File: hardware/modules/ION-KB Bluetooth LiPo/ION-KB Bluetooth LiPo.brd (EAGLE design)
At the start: 38.1 x 54.8 mm, 4 parts, among them IC1 BLUETOOTH-RN42", U1 MCP73831

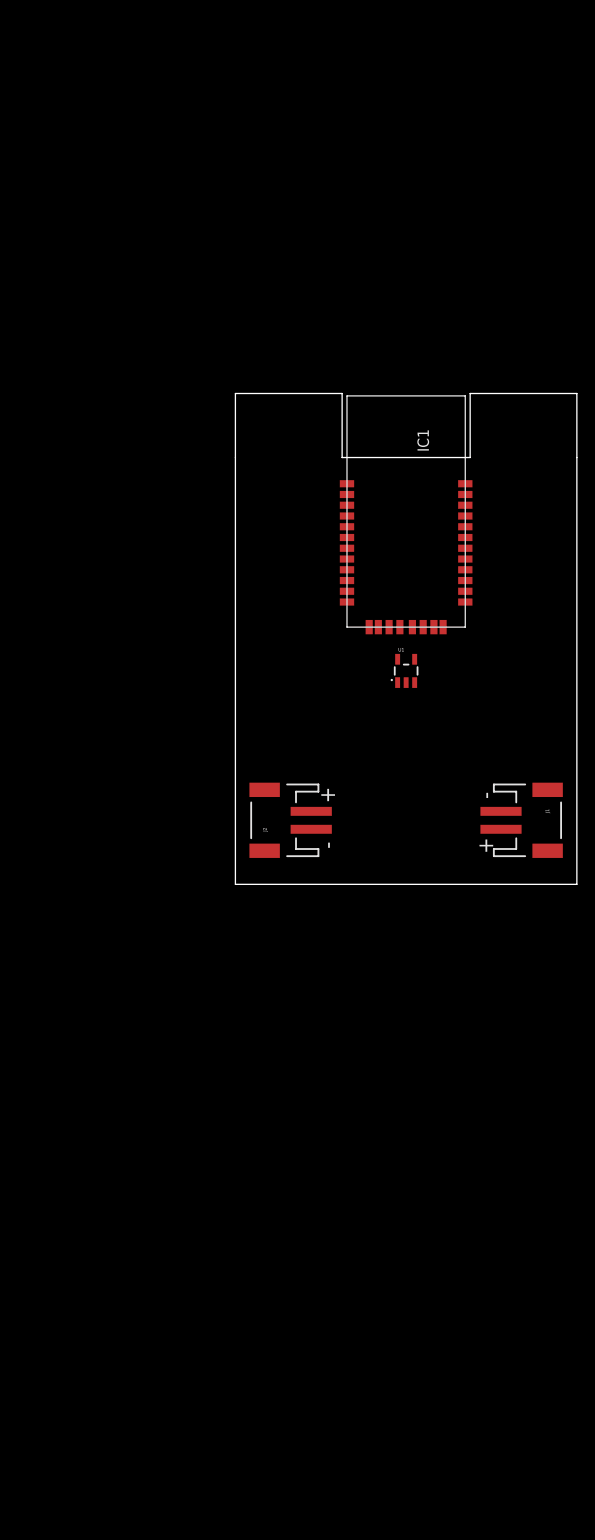
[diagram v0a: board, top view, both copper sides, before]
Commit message: Update bluetooth module
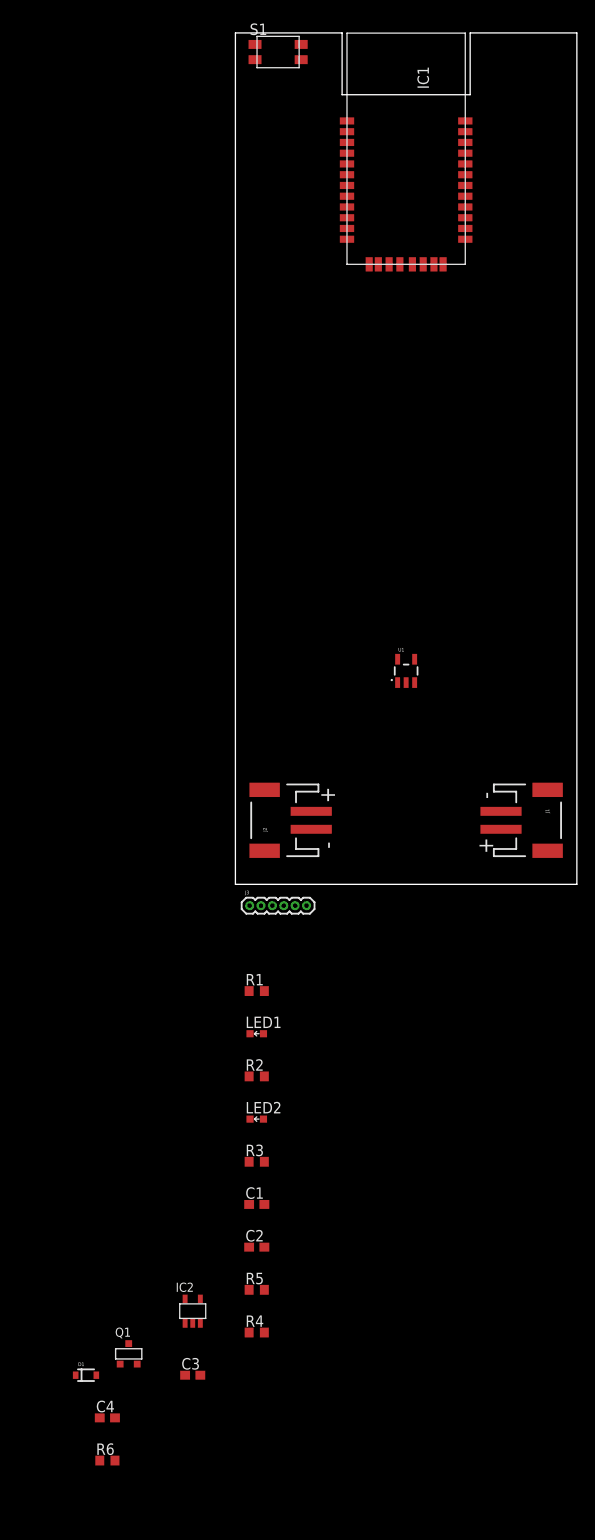
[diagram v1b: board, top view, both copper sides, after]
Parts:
- added C1, C2: 10uF, Jordi:C0603
- added C3: 470pF, Jordi:C0603
- added C4: 1uF, Jordi:C0603
- added D1: BAT20J, SparkFun-DiscreteSemi:SOD-323
- added IC2: VREG-5SOT23, Jordi:SOT23-5
- added J3: (no value), Jordi:M-1X06-0.05-PTH
- added LED1: Red, Jordi:L0603
- added LED2: Green, Jordi:L0603
- added Q1: MOSFET-PSUPERSOT, Jordi:SUPERSOT-3
- added R1, R4, R5: 10K, Jordi:R0603
- added R2, R3: 1K, Jordi:R0603
- added R6: 100K, Jordi:R0603
- added S1: (no value), Jordi:SWITCH-TACTILE-SMD
- moved IC1 40.5 mm to (19.1, 78.6)
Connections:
- removed net GND1: IC1.12
- removed net GND4: IC1.28
- removed net GND5: IC1.29
- removed net VDD: IC1.11
- removed net VSS: U1.2
- new net +3V3: IC1.11, IC2.4, J3.6, R5.2
- new net N$1: IC1.22, R1.2, S1.3, S1.4
- new net N$2: LED1.C, R2.2
- new net N$3: IC1.21, LED1.A
- new net N$4: IC1.19, LED2.A
- new net N$5: LED2.C, R3.2
- new net N$6: R4.1, U1.5
- new net N$8: C3.1, IC2.3
- new net STAT: R5.1, U1.1
- new net VCC: C4.2, D1.C, IC2.1, IC2.5, Q1.2
- net GND: now also C1.2, C2.1, C3.2, C4.1, IC1.12, IC1.28, IC1.29, IC2.2, J1.1, J2.1, J3.1, R1.1, R2.1, R3.1, R4.2, R6.1, S1.1, S1.2, U1.2
- net VBAT: now also C1.1, J1.2, J2.2, Q1.3
- net VIN: now also C2.2, D1.A, J3.5, Q1.1, R6.2
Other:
- board size 38.1 x 54.8 mm -> 38.1 x 95 mm

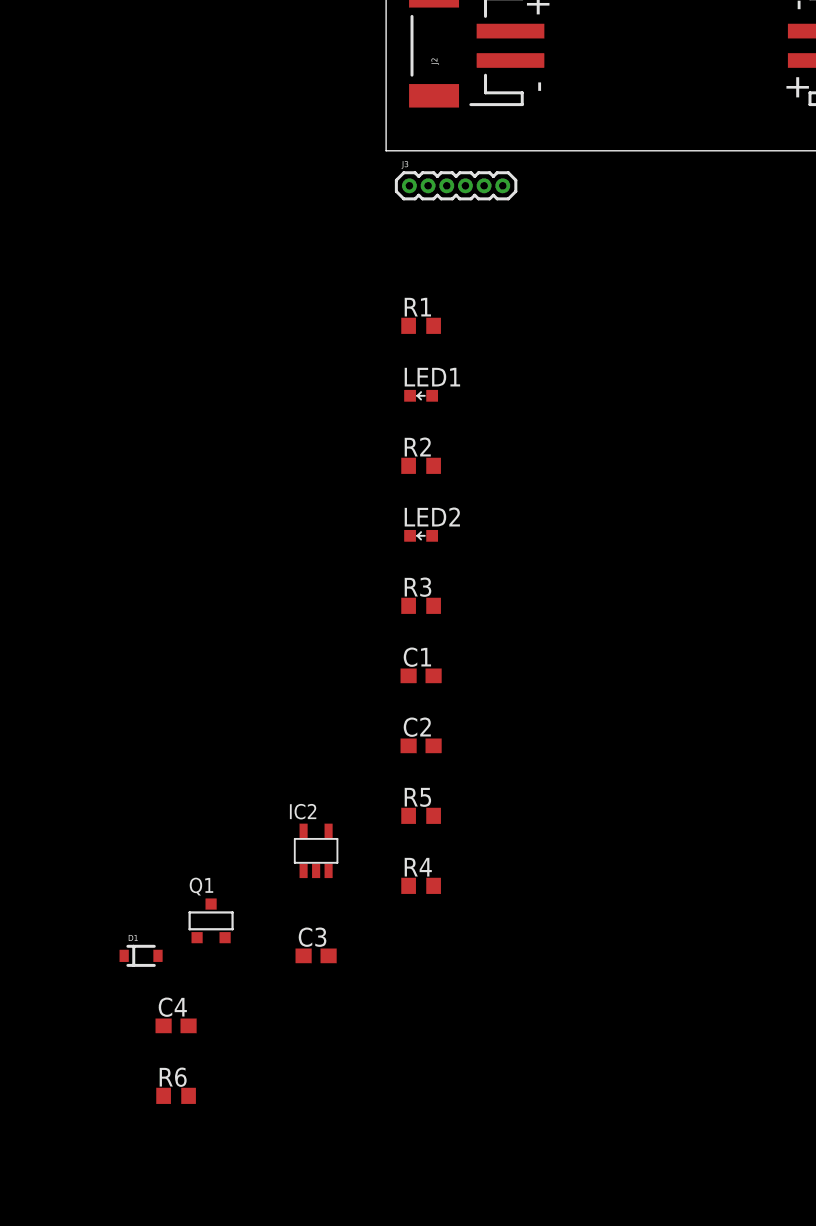
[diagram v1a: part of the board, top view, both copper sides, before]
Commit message: Remove VREG from Bluetooth board
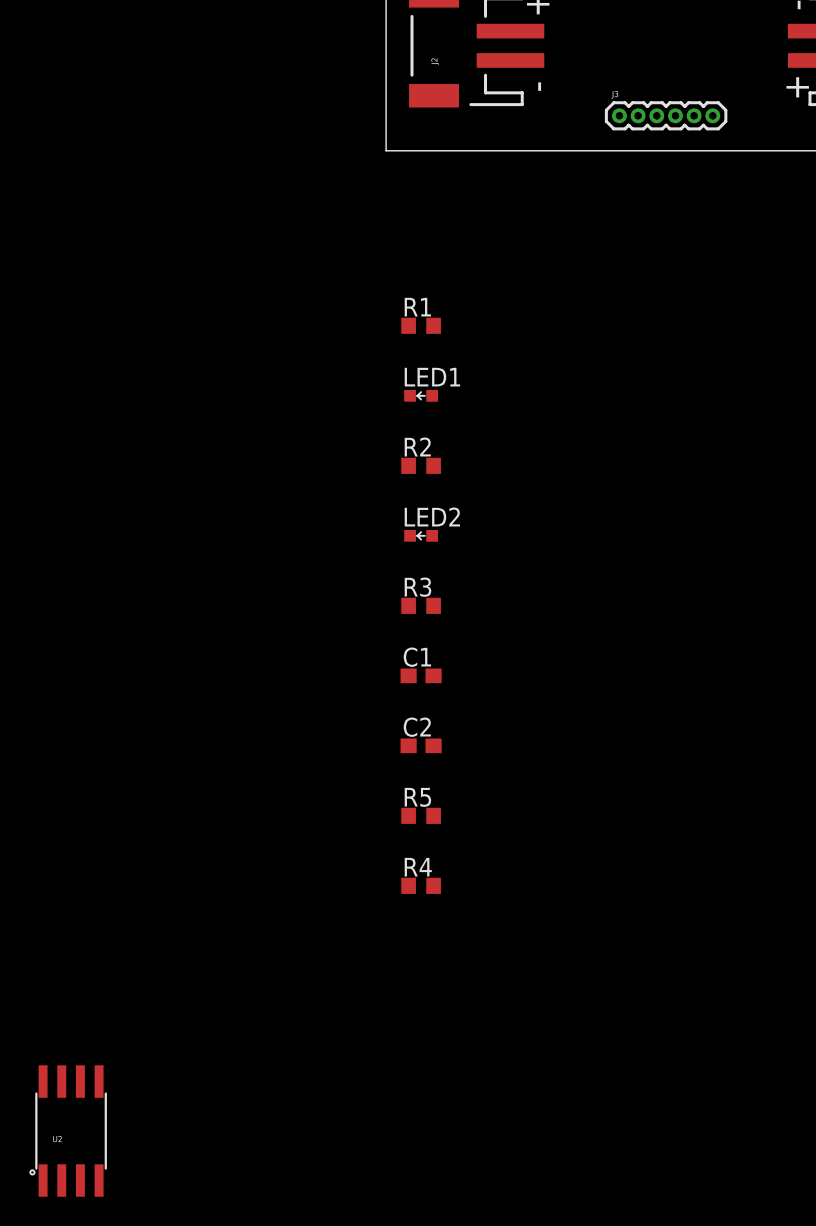
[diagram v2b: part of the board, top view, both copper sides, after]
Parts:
- removed C3: 470pF, Jordi:C0603
- removed C4: 1uF, Jordi:C0603
- removed D1: BAT20J, SparkFun-DiscreteSemi:SOD-323
- removed IC2: VREG-5SOT23, Jordi:SOT23-5
- removed Q1: MOSFET-PSUPERSOT, Jordi:SUPERSOT-3
- removed R6: 100K, Jordi:R0603
- added U2: Tiny85-20-SMT, SparkFun-DigitalIC:SO08-EIAJ
- moved J3 15.1 mm to (19.1, 2.38)
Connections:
- removed net N$8: C3.1, IC2.3
- removed net VCC: C4.2, D1.C, IC2.1, IC2.5, Q1.2
- new net RX: J3.3
- new net TX: J3.4
- net +3V3: no longer IC2.4
- net GND: no longer C3.2, C4.1, IC2.2, R6.1
- net VBAT: now also J3.2; no longer Q1.3
- net VIN: no longer D1.A, Q1.1, R6.2
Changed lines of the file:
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@@
 <attribute name="PROD_ID" value="IC-09995" x="19.05" y="23.8125" size="1.778" layer="27" display="off"/>
 </element>
-<element name="J3" library="Jordi" package="M-1X06-0.05-PTH" value="" x="4.7625" y="-2.38125"/>
+<element name="J3" library="Jordi" package="M-1X06-0.05-PTH" value="" x="19.05" y="2.38125"/>
 <element name="S1" library="Jordi" package="SWITCH-TACTILE-SMD" value="" x="4.7625" y="92.86875"/>
 <element name="R1" library="Jordi" package="R0603" value="10K" x="2.38125" y="-11.90625"/>
@@
 <element name="R5" library="Jordi" package="R0603" value="10K" x="2.38125" y="-45.24375"/>
 <element name="R4" library="Jordi" package="R0603" value="10K" x="2.38125" y="-50.00625"/>
-<element name="IC2" library="Jordi" package="SOT23-5" value="VREG-5SOT23" x="-4.7625" y="-47.625"/>
-<element name="C3" library="Jordi" package="C0603" value="470pF" x="-4.7625" y="-54.76875"/>
-<element name="Q1" library="Jordi" package="SUPERSOT-3" value="MOSFET-PSUPERSOT" x="-11.90625" y="-52.3875"/>
-<element name="D1" library="SparkFun-DiscreteSemi" package="SOD-323" value="BAT20J" x="-16.66875" y="-54.76875">
-<attribute name="PROD_ID" value="DIO-11623" x="-16.66875" y="-54.76875" size="1.778" layer="27" display="off"/>
+<element name="U2" library="SparkFun-DigitalIC" package="SO08-EIAJ" value="Tiny85-20-SMT" x="-21.43125" y="-66.675">
+<attribute name="PROD_ID" value="IC-09092" x="-21.43125" y="-66.675" size="1.778" layer="27" display="off"/>
 </element>
-<element name="C4" library="Jordi" package="C0603" value="1uF" x="-14.2875" y="-59.53125"/>
-<element name="R6" library="Jordi" package="R0603" value="100K" x="-14.2875" y="-64.29375"/>
 </elements>
 <signals>
@@
 <contactref element="C2" pad="1"/>
 <contactref element="R4" pad="2"/>
-<contactref element="IC2" pad="2"/>
-<contactref element="IC2" pad="2"/>
 <contactref element="C1" pad="2"/>
-<contactref element="C3" pad="2"/>
-<contactref element="C4" pad="1"/>
-<contactref element="R6" pad="1"/>
 <wire x1="7.3375" y1="92.01875" x2="7.3375" y2="93.71875" width="0" layer="19" extent="1-1"/>
 <wire x1="12.45" y1="85.18125" x2="7.3375" y2="92.01875" width="0" layer="19" extent="1-1"/>
@@
 <wire x1="29.6375" y1="8.14375" x2="19.05" y2="22.5124" width="0" layer="19" extent="1-1"/>
 <wire x1="8.4625" y1="6.14375" x2="19.05" y2="22.5124" width="0" layer="19" extent="1-1"/>
-<wire x1="1.5875" y1="-2.38125" x2="8.4625" y2="6.14375" width="0" layer="19" extent="1-1"/>
-<wire x1="1.53125" y1="-11.90625" x2="1.5875" y2="-2.38125" width="0" layer="19" extent="1-1"/>
+<wire x1="15.875" y1="2.38125" x2="8.4625" y2="6.14375" width="0" layer="19" extent="1-1"/>
+<wire x1="1.53125" y1="-11.90625" x2="15.875" y2="2.38125" width="0" layer="19" extent="1-1"/>
 <wire x1="1.53125" y1="-21.43125" x2="1.53125" y2="-11.90625" width="0" layer="19" extent="1-1"/>
 <wire x1="1.53125" y1="-30.95625" x2="1.53125" y2="-21.43125" width="0" layer="19" extent="1-1"/>
@@
 <wire x1="1.53125" y1="-40.48125" x2="3.23125" y2="-35.71875" width="0" layer="19" extent="1-1"/>
 <wire x1="3.23125" y1="-50.00625" x2="1.53125" y2="-40.48125" width="0" layer="19" extent="1-1"/>
-<wire x1="-4.7625" y1="-48.975" x2="3.23125" y2="-50.00625" width="0" layer="19" extent="1-1"/>
-<wire x1="-3.9125" y1="-54.76875" x2="-4.7625" y2="-48.975" width="0" layer="19" extent="1-1"/>
-<wire x1="-15.1375" y1="-59.53125" x2="-3.9125" y2="-54.76875" width="0" layer="19" extent="1-1"/>
-<wire x1="-15.1375" y1="-64.29375" x2="-15.1375" y2="-59.53125" width="0" layer="19" extent="1-1"/>
 </signal>
 <signal name="VBAT">
@@
 <contactref element="U1" pad="3"/>
 <contactref element="U1" pad="3"/>
-<contactref element="Q1" pad="3"/>
-<wire x1="1.53125" y1="-35.71875" x2="-11.90625" y2="-51.2445" width="0" layer="19" extent="1-1"/>
-<wire x1="8.4625" y1="8.14375" x2="1.53125" y2="-35.71875" width="0" layer="19" extent="1-1"/>
-<wire x1="20" y1="22.5124" x2="8.4625" y2="8.14375" width="0" layer="19" extent="1-1"/>
+<contactref element="J3" pad="2"/>
+<wire x1="8.4625" y1="8.14375" x2="20" y2="22.5124" width="0" layer="19" extent="1-1"/>
+<wire x1="17.145" y1="2.38125" x2="8.4625" y2="8.14375" width="0" layer="19" extent="1-1"/>
 <wire x1="29.6375" y1="6.14375" x2="20" y2="22.5124" width="0" layer="19" extent="1-1"/>
+<wire x1="1.53125" y1="-35.71875" x2="17.145" y2="2.38125" width="0" layer="19" extent="1-1"/>
 </signal>
 <signal name="+3V3">
 <contactref element="J3" pad="6"/>
 <contactref element="IC1" pad="11"/>
-<contactref element="IC2" pad="4"/>
 <contactref element="R5" pad="2"/>
-<wire x1="7.9375" y1="-2.38125" x2="12.45" y2="73.18125" width="0" layer="19" extent="1-1"/>
-<wire x1="3.23125" y1="-45.24375" x2="7.9375" y2="-2.38125" width="0" layer="19" extent="1-1"/>
-<wire x1="-3.9125" y1="-46.275" x2="3.23125" y2="-45.24375" width="0" layer="19" extent="1-1"/>
+<wire x1="22.225" y1="2.38125" x2="12.45" y2="73.18125" width="0" layer="19" extent="1-1"/>
+<wire x1="3.23125" y1="-45.24375" x2="22.225" y2="2.38125" width="0" layer="19" extent="1-1"/>
 </signal>
 <signal name="N$1">
@@
 <contactref element="C2" pad="2"/>
 <contactref element="J3" pad="5"/>
-<contactref element="D1" pad="A"/>
-<contactref element="Q1" pad="1"/>
-<contactref element="R6" pad="2"/>
-<wire x1="-15.51875" y1="-54.76875" x2="-13.4375" y2="-64.29375" width="0" layer="19" extent="1-1"/>
-<wire x1="-12.85875" y1="-53.5305" x2="-15.51875" y2="-54.76875" width="0" layer="19" extent="1-1"/>
-<wire x1="3.23125" y1="-40.48125" x2="-12.85875" y2="-53.5305" width="0" layer="19" extent="1-1"/>
-<wire x1="6.6675" y1="-2.38125" x2="3.23125" y2="-40.48125" width="0" layer="19" extent="1-1"/>
-<wire x1="20" y1="25.1126" x2="6.6675" y2="-2.38125" width="0" layer="19" extent="1-1"/>
+<wire x1="20.955" y1="2.38125" x2="20" y2="25.1126" width="0" layer="19" extent="1-1"/>
+<wire x1="3.23125" y1="-40.48125" x2="20.955" y2="2.38125" width="0" layer="19" extent="1-1"/>
 </signal>
 <signal name="N$6">
@@
 <wire x1="18.1" y1="25.1126" x2="1.53125" y2="-50.00625" width="0" layer="19" extent="1-1"/>
 </signal>
-<signal name="VCC">
-<contactref element="IC2" pad="1"/>
-<contactref element="IC2" pad="5"/>
-<contactref element="Q1" pad="2"/>
-<contactref element="D1" pad="C"/>
-<contactref element="C4" pad="2"/>
-<wire x1="-13.4375" y1="-59.53125" x2="-17.81875" y2="-54.76875" width="0" layer="19" extent="1-1"/>
-<wire x1="-10.95375" y1="-53.5305" x2="-13.4375" y2="-59.53125" width="0" layer="19" extent="1-1"/>
-<wire x1="-5.6125" y1="-48.975" x2="-10.95375" y2="-53.5305" width="0" layer="19" extent="1-1"/>
-<wire x1="-5.6125" y1="-46.275" x2="-5.6125" y2="-48.975" width="0" layer="19" extent="1-1"/>
+<signal name="TX">
+<contactref element="J3" pad="4"/>
 </signal>
-<signal name="N$8">
-<contactref element="IC2" pad="3"/>
-<contactref element="C3" pad="1"/>
-<wire x1="-3.9125" y1="-48.975" x2="-5.6125" y2="-54.76875" width="0" layer="19" extent="1-1"/>
+<signal name="RX">
+<contactref element="J3" pad="3"/>
 </signal>
 </signals>
